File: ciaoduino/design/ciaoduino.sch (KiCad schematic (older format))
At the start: 9 parts, among them P1 ICSP, SW1 SW_PUSH, SW2 SW_PUSH, U1 ATMEGA32U4-A, X1 CRYSTAL_SMD

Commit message: Add protocol connectors.
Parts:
- removed U1: ATMEGA32U4-A, TQFP44, symbol ATMEGA32U4-A
- added P2: CONN_01X02, Pin_Headers:Pin_Header_Angled_1x02, symbol CONN_01X02
- added P3: USB_OTG, Connect:USB_Mini-B, symbol USB_OTG
- added P4: CONN_01X06, Pin_Headers:Pin_Header_Angled_1x06, symbol CONN_01X06
- added P5: CONN_01X06, Pin_Headers:Pin_Header_Straight_1x06, symbol CONN_01X06
- added R3, R4: R, Resistors_SMD:R_0603, symbol R
- added U2: ATmega32U4-AU, Housings_QFP:TQFP-44_10x10mm_Pitch0.8mm, symbol ATmega32U4-AU
- R1: footprint Resistors_SMD:R_0603_HandSoldering -> Resistors_SMD:R_0603
- SW1: footprint Buttons_Switches_SMD:SW_SP3T_PCM13 -> Buttons_Switches_SMD:SW_SPST_KMR2
- SW2: footprint Buttons_Switches_SMD:SW_SP3T_PCM13 -> Buttons_Switches_SMD:SW_SPST_EVQP0
- X1: footprint Crystals:Crystal_SMD_0603_4Pads -> Crystals:Crystal_SMD_0603_2Pads_obsolete
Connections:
- net labels added: MOSI, SCLK, SS, usart_cts, usart_rts, usart_rx, usart_tx
- wire segments 19 -> 64
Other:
- moved on the sheet: C1, C2, R1, R2, SW1, SW2, X1

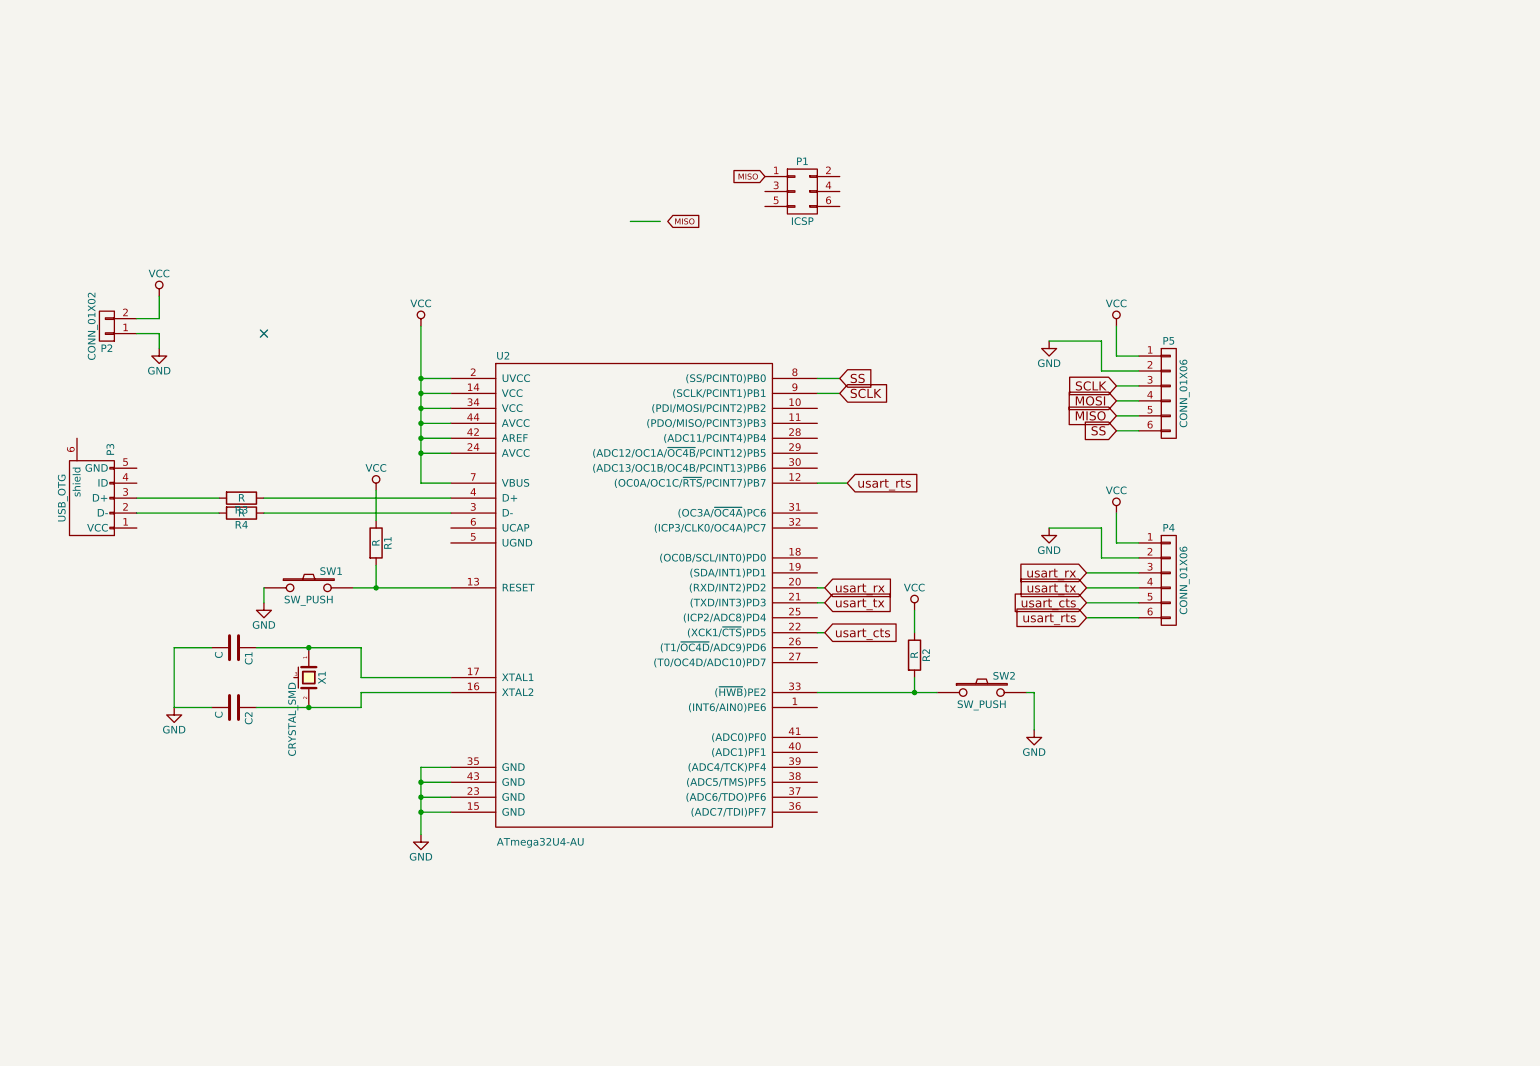
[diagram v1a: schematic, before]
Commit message: Route ADC related IO pins.
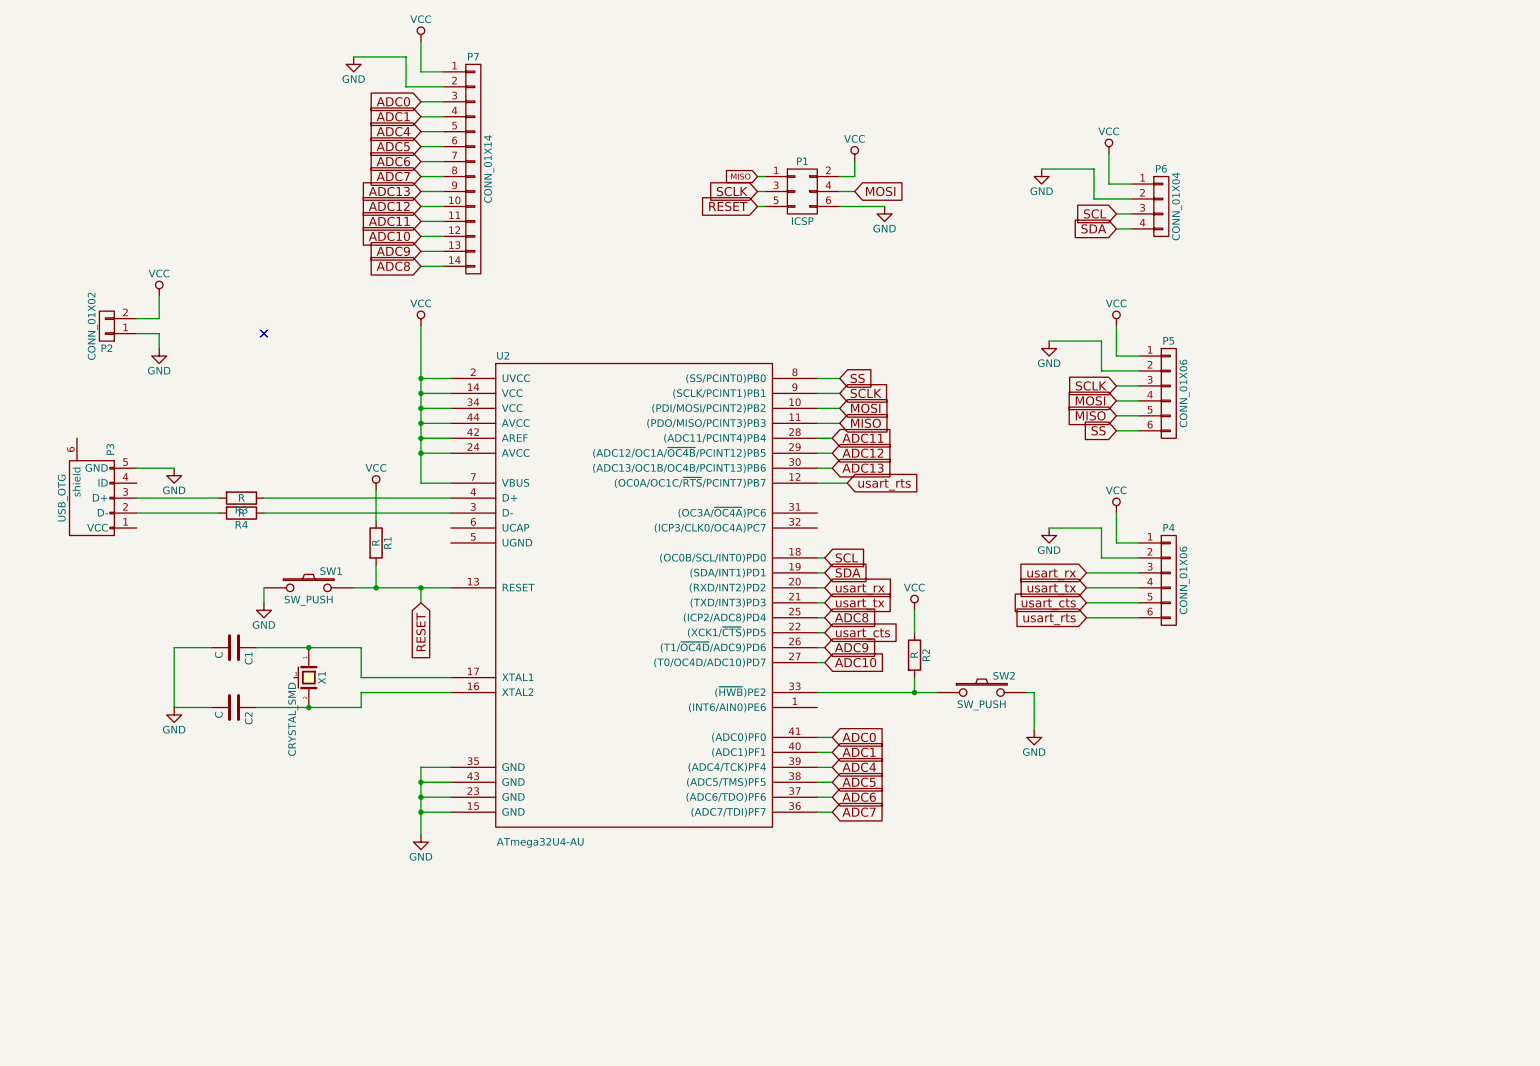
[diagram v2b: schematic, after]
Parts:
- added P6: CONN_01X04, Pin_Headers:Pin_Header_Straight_1x04, symbol CONN_01X04
- added P7: CONN_01X14, Pin_Headers:Pin_Header_Straight_1x14, symbol CONN_01X14
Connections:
- net GND: now also P1.6 (P6), P3.5 (GND), P6.2 (P2), P7.2 (P2)
- net MISO: now also U2.11 ((PDO/MISO/PCINT3)PB3)
- net MOSI: now also P1.4 (P4), U2.10 ((PDI/MOSI/PCINT2)PB2)
- net SCLK: now also P1.3 (P3)
- net VCC: now also P1.2 (P2), P6.1 (P1), P7.1 (P1)
- net RESET: now reaches P1.5 (P5)
- net RESET: now also R1.2, SW1.2, U2.13 (RESET)
- net SCL: now reaches U2.18 ((OC0B/SCL/INT0)PD0)
- net SCL: now also P6.3 (P3)
- net SDA: now reaches U2.19 ((SDA/INT1)PD1)
- net SDA: now also P6.4 (P4)
- net ADC8: now reaches U2.25 ((ICP2/ADC8)PD4)
- net ADC8: now also P7.14 (P14)
- net ADC9: now reaches U2.26 ((T1/~OC4D~/ADC9)PD6)
- net ADC9: now also P7.13 (P13)
- net ADC10: now reaches U2.27 ((T0/OC4D/ADC10)PD7)
- net ADC10: now also P7.12 (P12)
- net ADC11: now reaches U2.28 ((ADC11/PCINT4)PB4)
- net ADC11: now also P7.11 (P11)
- net ADC12: now reaches U2.29 ((ADC12/OC1A/~OC4B~/PCINT12)PB5)
- net ADC12: now also P7.10 (P10)
- net ADC13: now reaches U2.30 ((ADC13/OC1B/OC4B/PCINT13)PB6)
- net ADC13: now also P7.9 (P9)
- net ADC7: now reaches U2.36 ((ADC7/TDI)PF7)
- net ADC7: now also P7.8 (P8)
- net ADC6: now reaches U2.37 ((ADC6/TDO)PF6)
- net ADC6: now also P7.7 (P7)
- net ADC5: now reaches U2.38 ((ADC5/TMS)PF5)
- net ADC5: now also P7.6 (P6)
- net ADC4: now reaches U2.39 ((ADC4/TCK)PF4)
- net ADC4: now also P7.5 (P5)
- net ADC1: now reaches U2.40 ((ADC1)PF1)
- net ADC1: now also P7.4 (P4)
- net ADC0: now reaches U2.41 ((ADC0)PF0)
- net ADC0: now also P7.3 (P3)

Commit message: Rework layout.
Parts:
- X1: footprint Crystals:Crystal_SMD_0603_2Pads_obsolete -> Crystals:crystal_FA238-TSX3225
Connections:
- net GND: now also X1.3 (case)
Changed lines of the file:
@@
 F 0 "X1" H 2450 5040 50  0000 C CNN
 F 1 "CRYSTAL_SMD" H 2480 4840 50  0000 L CNN
-F 2 "Crystals:Crystal_SMD_0603_2Pads_obsolete" H 2450 4950 50  0001 C CNN
+F 2 "Crystals:crystal_FA238-TSX3225" H 2450 4950 50  0001 C CNN
 F 3 "" H 2450 4950 50  0000 C CNN
 	1    2450 4950
@@
 Wire Wire Line
 	3200 2200 3350 2200
+Wire Wire Line
+	2350 4950 1550 4950
+Connection ~ 1550 4950
 $EndSCHEMATC

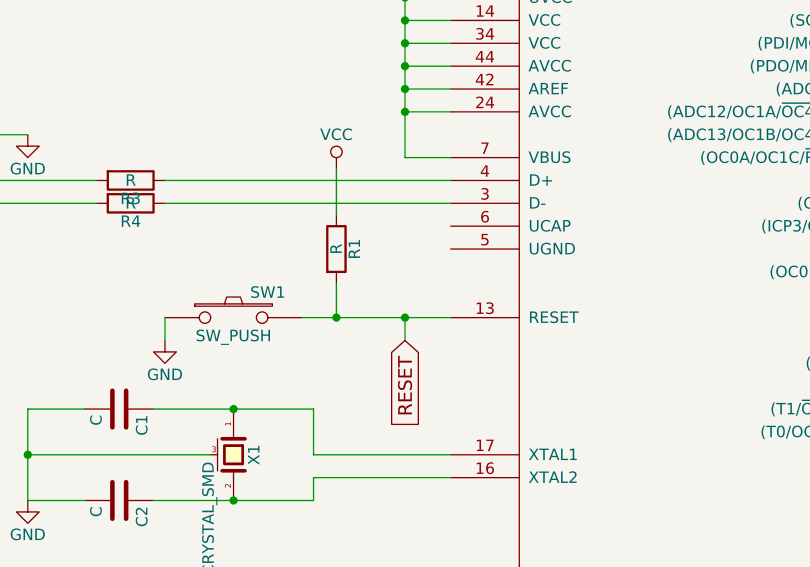
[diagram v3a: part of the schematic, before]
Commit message: Update board with UCAP pad connected.
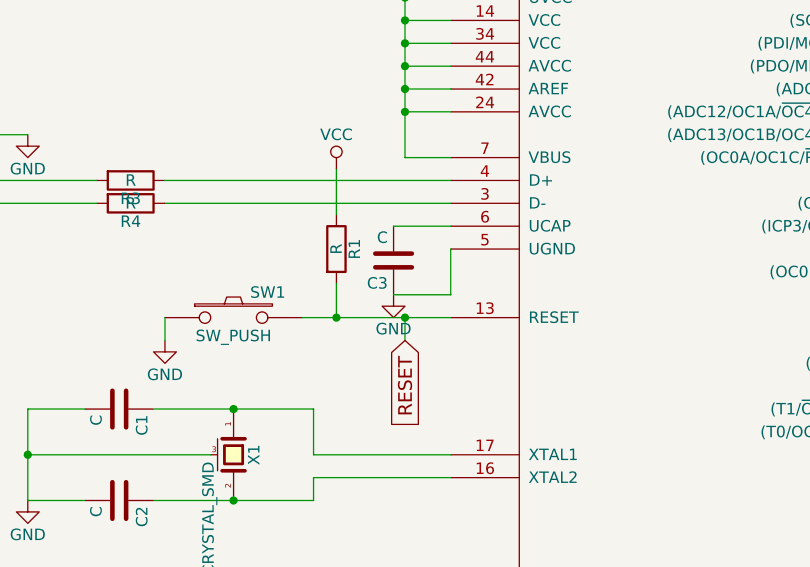
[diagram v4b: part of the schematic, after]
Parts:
- added C3: C, Capacitors_SMD:C_0603_HandSoldering, symbol C
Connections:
- net GND: now also U2.5 (UGND), C3.1
- net at U2.6 (UCAP): now also C3.2
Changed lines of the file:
@@
 	2350 4950 1550 4950
 Connection ~ 1550 4950
+$Comp
+L C C3
+U 1 1 578798AA
+P 3150 4100
+F 0 "C3" H 3175 4200 50  0000 L CNN
+F 1 "C" H 3175 4000 50  0000 L CNN
+F 2 "Capacitors_SMD:C_0603_HandSoldering" H 3188 3950 50  0001 C CNN
+F 3 "" H 3150 4100 50  0000 C CNN
+	1    3150 4100
+	-1   0    0    1
+$EndComp
+Wire Wire Line
+	3400 3950 3150 3950
+$Comp
+L GND #PWR021
+U 1 1 578799DA
+P 3150 4250
+F 0 "#PWR021" H 3150 4000 50  0001 C CNN
+F 1 "GND" H 3150 4100 50  0000 C CNN
+F 2 "" H 3150 4250 50  0000 C CNN
+F 3 "" H 3150 4250 50  0000 C CNN
+	1    3150 4250
+	1    0    0    -1
+$EndComp
+Wire Wire Line
+	3400 4050 3400 4250
+Wire Wire Line
+	3400 4250 3150 4250
 $EndSCHEMATC

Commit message: Rework layout.
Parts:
- P4: footprint Pin_Headers:Pin_Header_Angled_1x06 -> Pin_Headers:Pin_Header_Straight_1x06
- SW2: footprint Buttons_Switches_SMD:SW_SPST_EVQP0 -> Buttons_Switches_SMD:SW_SPST_KMR2
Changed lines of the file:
@@
 F 0 "SW2" H 7100 5160 50  0000 C CNN
 F 1 "SW_PUSH" H 6950 4970 50  0000 C CNN
-F 2 "Buttons_Switches_SMD:SW_SPST_EVQP0" H 6950 5050 50  0001 C CNN
+F 2 "Buttons_Switches_SMD:SW_SPST_KMR2" H 6950 5050 50  0001 C CNN
 F 3 "" H 6950 5050 50  0000 C CNN
 	1    6950 5050
@@
 F 0 "P4" H 8200 4650 50  0000 C CNN
 F 1 "CONN_01X06" V 8300 4300 50  0000 C CNN
-F 2 "Pin_Headers:Pin_Header_Angled_1x06" H 8200 4300 50  0001 C CNN
+F 2 "Pin_Headers:Pin_Header_Straight_1x06" H 8200 4300 50  0001 C CNN
 F 3 "" H 8200 4300 50  0000 C CNN
 	1    8200 4300

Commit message: ciaoduino: rework board.
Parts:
- added C4, C5: C, Capacitors_SMD:C_0603_HandSoldering, symbol C
- added Q1: Q_NMOS_DGS, TO_SOT_Packages_SMD:SOT-23, symbol Q_NMOS_DGS
- added U1: MCP1754ST-5002E/MB, TO_SOT_Packages_SMD:SOT-323, symbol MCP1754ST-5002E/MB
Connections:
- net GND: now also C4.1, C5.1, U1.2 (GND)
- net VCC: now also Q1.3 (S); no longer P2.2 (P2)
- net VCCUSB: now reaches P3.1 (VCC)
- net VCCUSB: now also Q1.1 (D)
- new net: C4.2, P2.2 (P2), U1.1 (VI)
- new net VIN: C5.2, Q1.2 (G), U1.3 (VO)
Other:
- moved on the sheet: P2
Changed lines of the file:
@@
 	1    0    0    -1
 $EndComp
-NoConn ~ 2150 2650
+NoConn ~ 1750 950
 $Comp
 L CRYSTAL_SMD X1
@@
 L CONN_01X02 P2
 U 1 1 57093081
-P 1100 2600
-F 0 "P2" H 1100 2750 50  0000 C CNN
-F 1 "CONN_01X02" V 1200 2600 50  0000 C CNN
-F 2 "Pin_Headers:Pin_Header_Angled_1x02" H 1100 2600 50  0001 C CNN
-F 3 "" H 1100 2600 50  0000 C CNN
-	1    1100 2600
+P 700 900
+F 0 "P2" H 700 1050 50  0000 C CNN
+F 1 "CONN_01X02" V 800 900 50  0000 C CNN
+F 2 "Pin_Headers:Pin_Header_Angled_1x02" H 700 900 50  0001 C CNN
+F 3 "" H 700 900 50  0000 C CNN
+	1    700  900
 	-1   0    0    1
 $EndComp
 $Comp
-L VCC #PWR08
-U 1 1 57093194
-P 1450 2400
-F 0 "#PWR08" H 1450 2250 50  0001 C CNN
-F 1 "VCC" H 1450 2550 50  0000 C CNN
-F 2 "" H 1450 2400 50  0000 C CNN
-F 3 "" H 1450 2400 50  0000 C CNN
-	1    1450 2400
-	1    0    0    -1
-$EndComp
-$Comp
-L GND #PWR09
+L GND #PWR08
 U 1 1 570931BD
-P 1450 2750
-F 0 "#PWR09" H 1450 2500 50  0001 C CNN
-F 1 "GND" H 1450 2600 50  0000 C CNN
-F 2 "" H 1450 2750 50  0000 C CNN
-F 3 "" H 1450 2750 50  0000 C CNN
-	1    1450 2750
+P 1050 1050
+F 0 "#PWR08" H 1050 800 50  0001 C CNN
+F 1 "GND" H 1050 900 50  0000 C CNN
+F 2 "" H 1050 1050 50  0000 C CNN
+F 3 "" H 1050 1050 50  0000 C CNN
+	1    1050 1050
 	1    0    0    -1
 $EndComp
@@
 $EndComp
 $Comp
-L VCC #PWR010
+L VCC #PWR09
 U 1 1 570969CE
 P 7850 2600
-F 0 "#PWR010" H 7850 2450 50  0001 C CNN
+F 0 "#PWR09" H 7850 2450 50  0001 C CNN
 F 1 "VCC" H 7850 2750 50  0000 C CNN
 F 2 "" H 7850 2600 50  0000 C CNN
@@
 $EndComp
 $Comp
-L GND #PWR011
+L GND #PWR010
 U 1 1 57096AFF
 P 7400 2700
-F 0 "#PWR011" H 7400 2450 50  0001 C CNN
+F 0 "#PWR010" H 7400 2450 50  0001 C CNN
 F 1 "GND" H 7400 2550 50  0000 C CNN
 F 2 "" H 7400 2700 50  0000 C CNN
@@
 SS
 $Comp
-L VCC #PWR012
+L VCC #PWR011
 U 1 1 570BE5B1
 P 7850 3850
-F 0 "#PWR012" H 7850 3700 50  0001 C CNN
+F 0 "#PWR011" H 7850 3700 50  0001 C CNN
 F 1 "VCC" H 7850 4000 50  0000 C CNN
 F 2 "" H 7850 3850 50  0000 C CNN
@@
 $EndComp
 $Comp
-L GND #PWR013
+L GND #PWR012
 U 1 1 570BE5B7
 P 7400 3950
-F 0 "#PWR013" H 7400 3700 50  0001 C CNN
+F 0 "#PWR012" H 7400 3700 50  0001 C CNN
 F 1 "GND" H 7400 3800 50  0000 C CNN
 F 2 "" H 7400 3950 50  0000 C CNN
@@
 $EndComp
 $Comp
-L VCC #PWR014
+L VCC #PWR013
 U 1 1 570BF036
 P 7800 1450
-F 0 "#PWR014" H 7800 1300 50  0001 C CNN
+F 0 "#PWR013" H 7800 1300 50  0001 C CNN
 F 1 "VCC" H 7800 1600 50  0000 C CNN
 F 2 "" H 7800 1450 50  0000 C CNN
@@
 $EndComp
 $Comp
-L GND #PWR015
+L GND #PWR014
 U 1 1 570BF03C
 P 7350 1550
-F 0 "#PWR015" H 7350 1300 50  0001 C CNN
+F 0 "#PWR014" H 7350 1300 50  0001 C CNN
 F 1 "GND" H 7350 1400 50  0000 C CNN
 F 2 "" H 7350 1550 50  0000 C CNN
@@
 MISO
 $Comp
-L VCC #PWR016
+L VCC #PWR015
 U 1 1 570C0497
 P 6100 1500
-F 0 "#PWR016" H 6100 1350 50  0001 C CNN
+F 0 "#PWR015" H 6100 1350 50  0001 C CNN
 F 1 "VCC" H 6100 1650 50  0000 C CNN
 F 2 "" H 6100 1500 50  0000 C CNN
@@
 $EndComp
 $Comp
-L GND #PWR017
+L GND #PWR016
 U 1 1 570C04D2
 P 6300 1800
-F 0 "#PWR017" H 6300 1550 50  0001 C CNN
+F 0 "#PWR016" H 6300 1550 50  0001 C CNN
 F 1 "GND" H 6300 1650 50  0000 C CNN
 F 2 "" H 6300 1800 50  0000 C CNN
@@
 RESET
 $Comp
-L GND #PWR018
+L GND #PWR017
 U 1 1 570C097B
 P 1550 3550
-F 0 "#PWR018" H 1550 3300 50  0001 C CNN
+F 0 "#PWR017" H 1550 3300 50  0001 C CNN
 F 1 "GND" H 1550 3400 50  0000 C CNN
 F 2 "" H 1550 3550 50  0000 C CNN
@@
 $EndComp
 $Comp
-L VCC #PWR019
+L VCC #PWR018
 U 1 1 570D5FF9
 P 3200 700
-F 0 "#PWR019" H 3200 550 50  0001 C CNN
+F 0 "#PWR018" H 3200 550 50  0001 C CNN
 F 1 "VCC" H 3200 850 50  0000 C CNN
 F 2 "" H 3200 700 50  0000 C CNN
@@
 $EndComp
 $Comp
-L GND #PWR020
+L GND #PWR019
 U 1 1 570D5FFF
 P 2750 800
-F 0 "#PWR020" H 2750 550 50  0001 C CNN
+F 0 "#PWR019" H 2750 550 50  0001 C CNN
 F 1 "GND" H 2750 650 50  0000 C CNN
 F 2 "" H 2750 800 50  0000 C CNN
@@
 	6500 4500 6500 4650
 Wire Wire Line
-	2800 4750 2100 4750
+	2100 4750 2800 4750
 Wire Wire Line
 	2800 5050 3400 5050
 Wire Wire Line
-	2800 5050 2800 5150
-Wire Wire Line
-	2800 5150 2100 5150
+	2800 5150 2800 5050
+Wire Wire Line
+	2100 5150 2800 5150
 Connection ~ 2450 4750
 Connection ~ 2450 5150
 Wire Wire Line
-	1800 5150 1550 5150
+	1550 5150 1800 5150
 Wire Wire Line
 	1800 4750 1550 4750
@@
 	2800 4950 3400 4950
 Wire Wire Line
-	2800 4950 2800 4750
+	2800 4750 2800 4950
 Wire Wire Line
 	3200 2600 3200 3650
@@
 Connection ~ 3200 2950
 Wire Wire Line
-	3200 6000 3200 5550
+	3200 5550 3200 6000
 Wire Wire Line
 	3200 5550 3400 5550
@@
 Connection ~ 3200 5850
 Wire Wire Line
-	1300 2550 1450 2550
-Wire Wire Line
-	1450 2550 1450 2400
-Wire Wire Line
-	1450 2750 1450 2650
-Wire Wire Line
-	1450 2650 1300 2650
+	900  850  1350 850
+Wire Wire Line
+	1050 1050 1050 950
+Wire Wire Line
+	1050 950  900  950
 Wire Wire Line
 	3400 3750 2150 3750
@@
 	3400 3950 3150 3950
 $Comp
-L GND #PWR021
+L GND #PWR020
 U 1 1 578799DA
 P 3150 4250
-F 0 "#PWR021" H 3150 4000 50  0001 C CNN
+F 0 "#PWR020" H 3150 4000 50  0001 C CNN
 F 1 "GND" H 3150 4100 50  0000 C CNN
 F 2 "" H 3150 4250 50  0000 C CNN
@@
 Wire Wire Line
 	3400 4250 3150 4250
+$Comp
+L GND #PWR021
+U 1 1 578D3B3C
+P 1650 1050
+F 0 "#PWR021" H 1650 800 50  0001 C CNN
+F 1 "GND" H 1650 900 50  0000 C CNN
+F 2 "" H 1650 1050 50  0000 C CNN
+F 3 "" H 1650 1050 50  0000 C CNN
+	1    1650 1050
+	1    0    0    -1
+$EndComp
+$Comp
+L C C4
+U 1 1 578D3C2E
+P 1250 1000
+F 0 "C4" H 1275 1100 50  0000 L CNN
+F 1 "C" H 1275 900 50  0000 L CNN
+F 2 "Capacitors_SMD:C_0603_HandSoldering" H 1288 850 50  0001 C CNN
+F 3 "" H 1250 1000 50  0000 C CNN
+	1    1250 1000
+	-1   0    0    1
+$EndComp
+$Comp
+L C C5
+U 1 1 578D3CDA
+P 2200 1000
+F 0 "C5" H 2225 1100 50  0000 L CNN
+F 1 "C" H 2225 900 50  0000 L CNN
+F 2 "Capacitors_SMD:C_0603_HandSoldering" H 2238 850 50  0001 C CNN
+F 3 "" H 2200 1000 50  0000 C CNN
+	1    2200 1000
+	-1   0    0    1
+$EndComp
+Connection ~ 1250 850
+Wire Wire Line
+	2200 850  1950 850
+$Comp
+L GND #PWR022
+U 1 1 578D3F2B
+P 1250 1150
+F 0 "#PWR022" H 1250 900 50  0001 C CNN
+F 1 "GND" H 1250 1000 50  0000 C CNN
+F 2 "" H 1250 1150 50  0000 C CNN
+F 3 "" H 1250 1150 50  0000 C CNN
+	1    1250 1150
+	1    0    0    -1
+$EndComp
+$Comp
+L GND #PWR023
+U 1 1 578D3F75
+P 2200 1150
+F 0 "#PWR023" H 2200 900 50  0001 C CNN
+F 1 "GND" H 2200 1000 50  0000 C CNN
+F 2 "" H 2200 1150 50  0000 C CNN
+F 3 "" H 2200 1150 50  0000 C CNN
+	1    2200 1150
+	1    0    0    -1
+$EndComp
+$Comp
+L Q_NMOS_DGS Q1
+U 1 1 578D412B
+P 1550 2500
+F 0 "Q1" H 1850 2550 50  0000 R CNN
+F 1 "Q_NMOS_DGS" H 2200 2450 50  0000 R CNN
+F 2 "TO_SOT_Packages_SMD:SOT-23" H 1750 2600 50  0001 C CNN
+F 3 "" H 1550 2500 50  0000 C CNN
+	1    1550 2500
+	0    1    1    0
+$EndComp
+Wire Wire Line
+	1300 3950 1500 3950
+Text GLabel 1500 3950 2    39   Input ~ 0
+VCCUSB
+Wire Wire Line
+	2200 850  2200 700
+Text GLabel 2200 700  2    60   Input ~ 0
+VIN
+Text GLabel 1550 2300 1    60   Input ~ 0
+VIN
+Text GLabel 1750 2600 2    60   Input ~ 0
+VCCUSB
+Text GLabel 1350 2600 0    60   Input ~ 0
+VCC
+$Comp
+L MCP1754ST-5002E/MB U1
+U 1 1 578D3A18
+P 1650 850
+F 0 "U1" H 1750 700 50  0000 C CNN
+F 1 "MCP1754ST-5002E/MB" H 1650 1000 50  0000 C CNN
+F 2 "TO_SOT_Packages_SMD:SOT-323" H 1650 850 50  0001 C CNN
+F 3 "" H 1650 850 50  0000 C CNN
+	1    1650 850
+	1    0    0    -1
+$EndComp
 $EndSCHEMATC
